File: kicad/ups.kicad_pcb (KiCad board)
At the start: 2 copper layers, 50 x 50 mm, 66 parts, among them J1 VIN, J2 Output, J3 Batt, J4 Conn_01x01, J5 NTC, J6 2S_MID, Q1 IRF7324, Q2 AO3401A, Q3 AO3401A, Q4 FDS6890A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

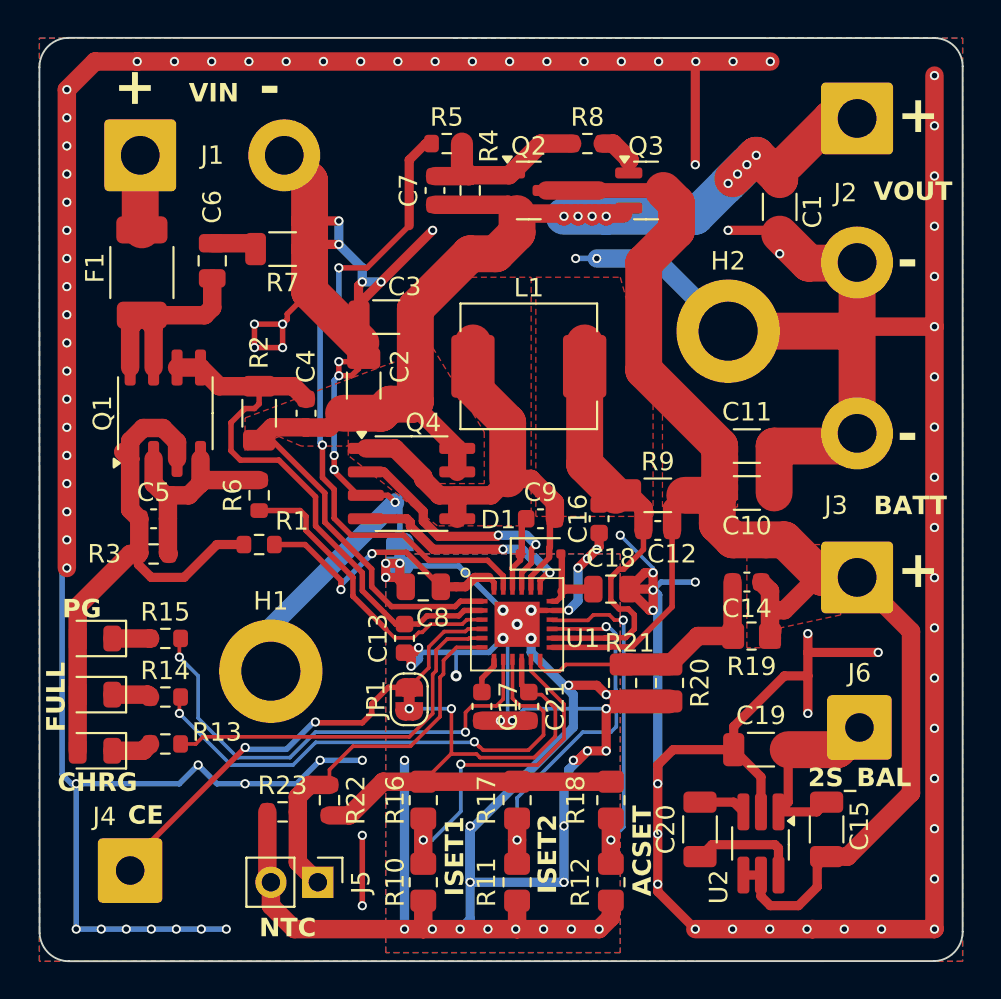
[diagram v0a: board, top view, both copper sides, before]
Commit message: Add recharge threshold control
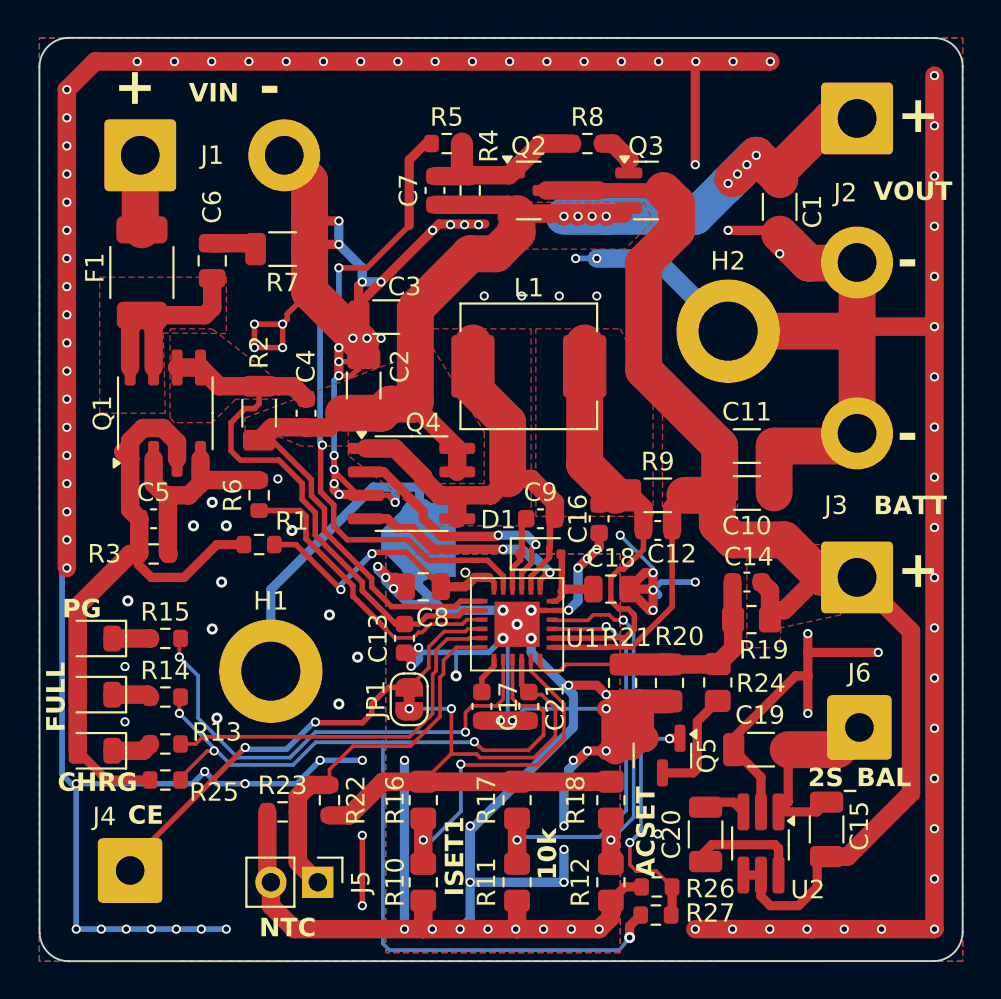
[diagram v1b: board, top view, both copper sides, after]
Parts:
- removed JP2: SolderJumper_2_Bridged, Jumper:SolderJumper-2_P1.3mm_Bridged_RoundedPad1.0x1.5mm
- added NT1: NetTie1, NetTie:NetTie-2_SMD_Pad2.0mm, B.Cu at (105.2, 70.4)
- added Q5: BSS138, Package_TO_SOT_SMD:SOT-23, F.Cu at (118.4, 82.0)
- added R24: 1M, Resistor_SMD:R_0805_2012Metric_Pad1.20x1.40mm_HandSolder, F.Cu at (121.4, 78.1)
- added R25: 1M, Resistor_SMD:R_0603_1608Metric, F.Cu at (91.4, 83.4)
- added R26: 1M, Resistor_SMD:R_0603_1608Metric, F.Cu at (118.1, 89.2)
- added R27: 1M, Resistor_SMD:R_0603_1608Metric, F.Cu at (118.0, 90.7)
- J1: value VIN -> Input
- R11: value ISET2 -> 10k
- moved R19 0.89 mm to (123.2, 74.7)
- moved C20 0.41 mm to (120.7, 86.3)
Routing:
- net /ST2: track 28.2 -> 57.1 mm, vias 2 -> 4
- net Net-(Q5-G): track 0.00 -> 13.1 mm, vias 0 -> 2
- net GND: track 142.7 -> 155.4 mm, vias 36 -> 37
- net Earth: track 343.4 -> 334.4 mm, vias 104 -> 129
- net Net-(Q5-D): track 0.00 -> 6.11 mm
- net Net-(D2-A): track 30.5 -> 35.1 mm
- net Net-(U1-ISET2): track 20.4 -> 22.5 mm
- net Net-(J3-Pin_1): track 86.6 -> 85.2 mm
- added copper zone on F.Cu, net Net-(C6-Pad1)
- added copper zone on F.Cu, net Net-(U1-ACP)

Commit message: Minor reroute
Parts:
- moved L1 1.96 mm to (112.4, 62.4)
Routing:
- net Earth: track 334.4 -> 350.9 mm, vias 129 -> 134
- net Net-(Q4A-S1): track 26.9 -> 21.8 mm
- net Net-(U1-SRP): track 25.0 -> 21.6 mm

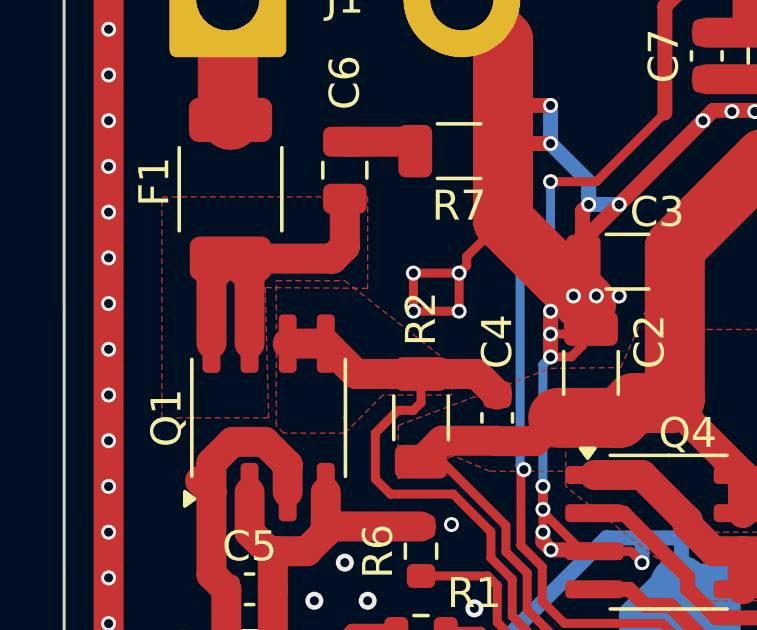
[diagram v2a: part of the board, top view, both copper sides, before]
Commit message: More copper for the input mosfet
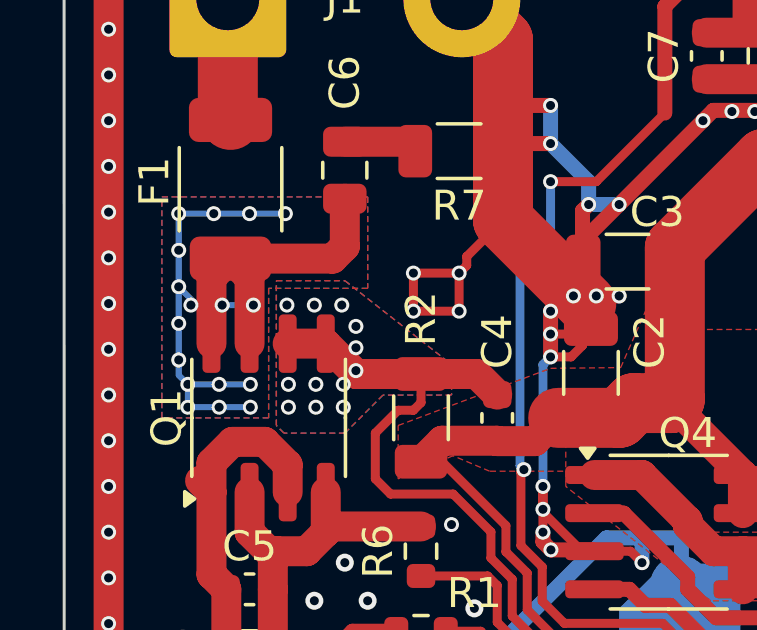
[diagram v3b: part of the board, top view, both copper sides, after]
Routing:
- net Net-(C6-Pad1): track 11.8 -> 28.8 mm, vias 0 -> 17
- net Net-(U1-ACP): vias 0 -> 12
- added copper zone on B.Cu, net Net-(C6-Pad1)
- added copper zone on B.Cu, net Net-(U1-ACP)

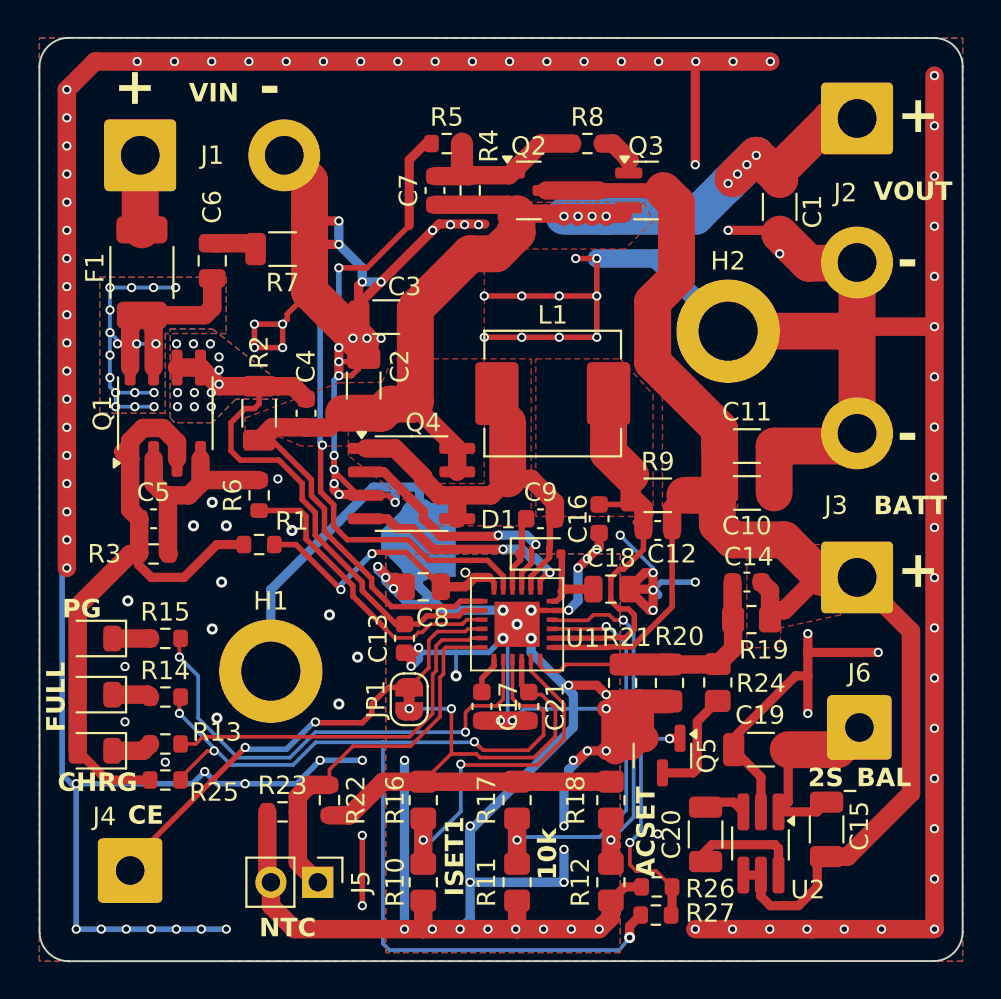
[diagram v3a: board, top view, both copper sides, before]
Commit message: Update part names, minor fix in the ground plane
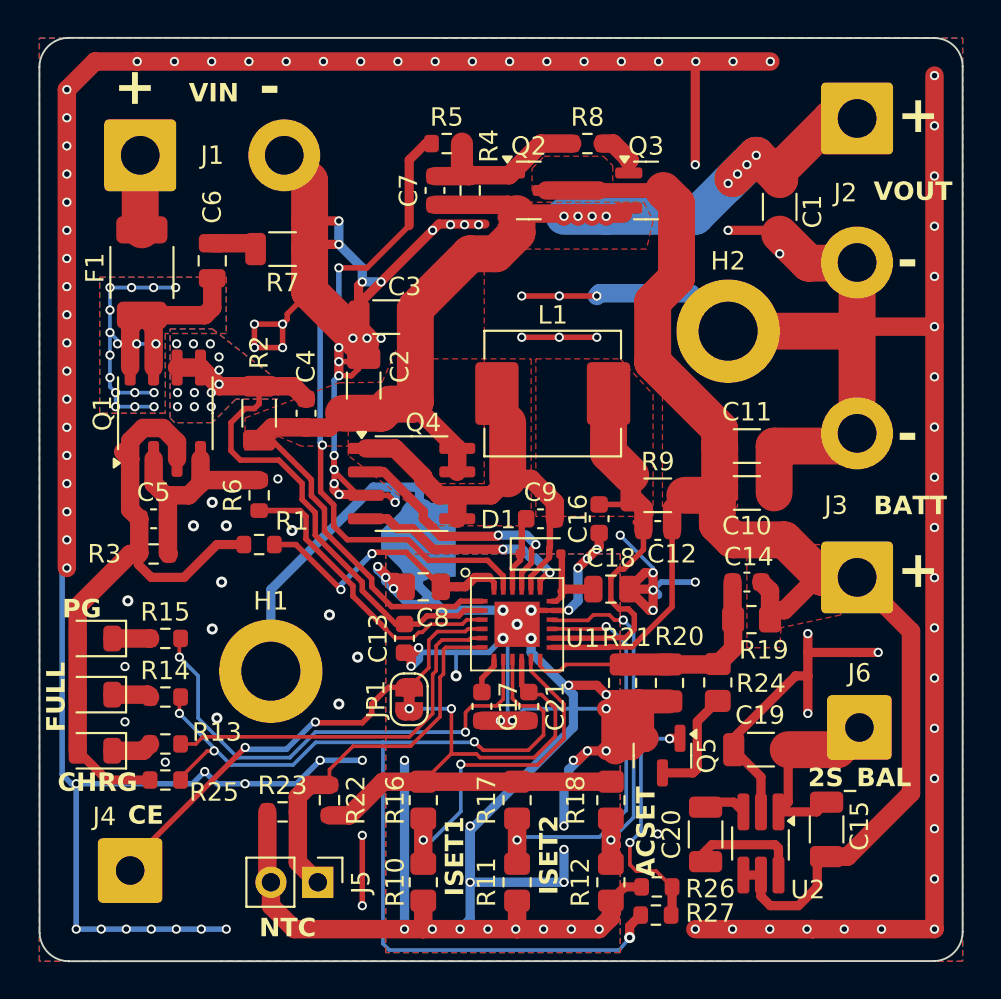
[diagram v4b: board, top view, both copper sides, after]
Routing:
- net Earth: track 350.9 -> 340.7 mm, vias 134 -> 130
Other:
- board text added: "ISET2"

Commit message: pcb: Update part names
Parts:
- Q1: value IRF7324 -> AO4801A
- Q4: value FDS6890A -> AO4800
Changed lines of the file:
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@@
 			)
 		)
-		(property "Value" "IRF7324"
+		(property "Value" "AO4801A"
 			(at 0 3.4 -90)
 			(layer "F.Fab")
@@
 			)
 		)
-		(property "Value" "FDS6890A"
+		(property "Value" "AO4800"
 			(at 0 3.4 0)
 			(layer "F.Fab")
@@
 	)
 	(zone
-		(net 32)
-		(net_name "Net-(Q4B-G2)")
-		(layer "F.Cu")
-		(name "$teardrop_padvia$")
-		(hatch full 0.1)
-		(priority 30064)
-		(attr
-			(teardrop
-				(type padvia)
-			)
-		)
-		(connect_pads yes
-			(clearance 0)
-		)
-		(min_thickness 0.0254)
-		(filled_areas_thickness no)
-		(fill yes
-			(thermal_gap 0.5)
-			(thermal_bridge_width 0.5)
-			(island_removal_mode 1)
-			(island_area_min 10)
-		)
-		(polygon
-			(pts
-				(xy 103.366006 69.469558) (xy 103.719558 69.116006) (xy 103.240536 68.973107) (xy 102.299293 69.214293)
-				(xy 103.125 69.515)
-			)
-		)
-	)
-	(zone
 		(net 20)
 		(net_name "Net-(JP1-A)")
@@
 	)
 	(zone
-		(net 10)
-		(net_name "Net-(U1-VCC)")
+		(net 32)
+		(net_name "Net-(Q4B-G2)")
 		(layer "F.Cu")
 		(name "$teardrop_padvia$")
 		(hatch full 0.1)
-		(priority 30089)
+		(priority 30001)
 		(attr
 			(teardrop
@@
 		(polygon
 			(pts
-				(xy 103.116665 71.178) (xy 103.116665 70.878) (xy 102.631818 70.854182) (xy 102.630818 71.104182)
-				(xy 102.727489 71.335152)
+				(xy 103.366006 69.469558) (xy 103.719558 69.116006) (xy 103.240536 68.973107) (xy 102.299293 69.214293)
+				(xy 103.125 69.515)
 			)
 		)
 	)
 	(zone
-		(net 7)
-		(net_name "Net-(C6-Pad2)")
+		(net 10)
+		(net_name "Net-(U1-VCC)")
 		(layer "F.Cu")
 		(name "$teardrop_padvia$")
 		(hatch full 0.1)
-		(priority 30031)
+		(priority 30089)
 		(attr
 			(teardrop
@@
 		(polygon
 			(pts
-				(xy 95.2025 53.795) (xy 95.2025 54.795) (xy 95.765 55.036456) (xy 96.3285 54.61) (xy 95.792891 53.876066)
+				(xy 103.116665 71.178) (xy 103.116665 70.878) (xy 102.631818 70.854182) (xy 102.630818 71.104182)
+				(xy 102.727489 71.335152)
 			)
 		)
 	)
 	(zone
-		(net 20)
-		(net_name "Net-(JP1-A)")
+		(net 7)
+		(net_name "Net-(C6-Pad2)")
 		(layer "F.Cu")
 		(name "$teardrop_padvia$")
 		(hatch full 0.1)
-		(priority 30124)
+		(priority 30031)
 		(attr
 			(teardrop
@@
 		(polygon
 			(pts
-				(xy 106.834 80.002) (xy 107.034 80.002) (xy 107.16497 79.597671) (xy 106.934 79.501) (xy 106.70303 79.597671)
+				(xy 95.2025 53.795) (xy 95.2025 54.795) (xy 95.765 55.036456) (xy 96.3285 54.61) (xy 95.792891 53.876066)
 			)
 		)
 	)
 	(zone
-		(net 31)
-		(net_name "Net-(Q4A-G1)")
+		(net 20)
+		(net_name "Net-(JP1-A)")
 		(layer "F.Cu")
 		(name "$teardrop_padvia$")
 		(hatch full 0.1)
-		(priority 30045)
+		(priority 30124)
 		(attr
 			(teardrop
@@
 		(polygon
 			(pts
-				(xy 103.310355 67.063909) (xy 103.663908 66.710356) (xy 103.275 66.544344) (xy 102.299293 66.674293)
-				(xy 102.276575 66.975)
+				(xy 106.834 80.002) (xy 107.034 80.002) (xy 107.16497 79.597671) (xy 106.934 79.501) (xy 106.70303 79.597671)
 			)
 		)
@@
 			)
 		)
+	)
+	(zone
+		(net 31)
+		(net_name "Net-(Q4A-G1)")
+		(layer "F.Cu")
+		(name "$teardrop_padvia$")
+		(hatch full 0.1)
+		(priority 30000)
+		(attr
+			(teardrop
+				(type padvia)
+			)
+		)
+		(connect_pads yes
+			(clearance 0)
+		)
+		(min_thickness 0.0254)
+		(filled_areas_thickness no)
+		(fill yes
+			(thermal_gap 0.5)
+			(thermal_bridge_width 0.5)
+			(island_removal_mode 1)
+			(island_area_min 10)
+		)
+		(polygon
+			(pts
+				(xy 103.310355 67.063909) (xy 103.663908 66.710356) (xy 103.275 66.544344) (xy 102.299293 66.674293)
+				(xy 102.276575 66.975)
+			)
+		)

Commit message: Update iBOM
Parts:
- R10: value 22.1k -> 22k
- R11: value 10k -> 16k
- R12: value 32.4k -> 22k
- R19: value 500k -> 390k
- R2, R9: value 22m -> 20m
- R20: value 200k -> 150k
- R21: value 200k -> 1.2M
